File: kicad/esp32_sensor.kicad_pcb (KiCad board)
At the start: 4 copper layers, 66 x 58.4 mm, 51 parts

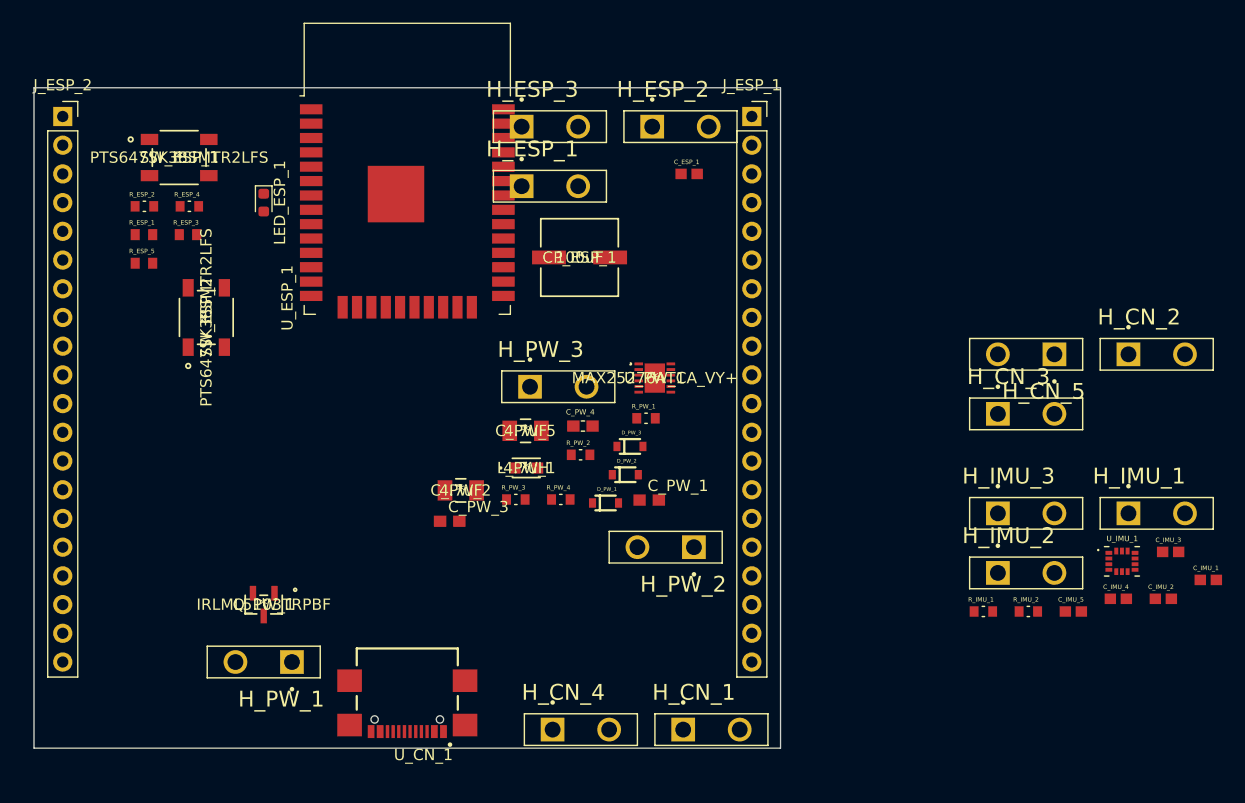
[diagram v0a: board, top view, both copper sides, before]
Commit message: Created PCB design for ESP32 sensor for v0.0.1. Exported PDFs and gerber files
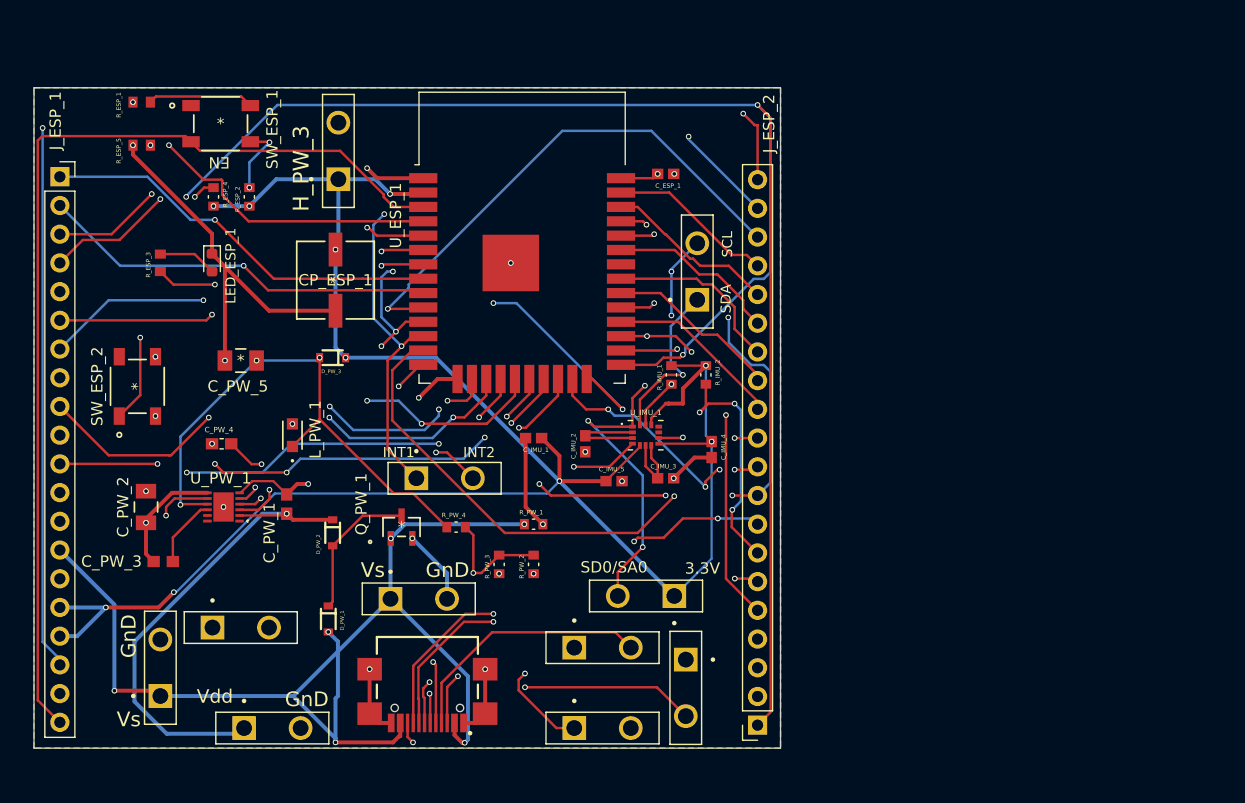
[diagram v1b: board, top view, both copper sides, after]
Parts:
- removed H_ESP_1, H_ESP_2, H_ESP_3: 1546931-2, footprints:1546931-2
- moved J_ESP_2 81.7 mm to (142.7, 125.0), turned to 180 degrees
- moved H_CN_3 79.8 mm to (89.9, 119.9), turned to 90 degrees
- moved H_CN_5 73.6 mm to (97.0, 116.3), turned to 0 degrees
- moved J_ESP_1 61.4 mm to (81.0, 76.5)
- moved C_IMU_1 61.0 mm to (122.9, 99.6), turned to 180 degrees
- moved C_IMU_2 52.9 mm to (127.5, 100.1), turned to 90 degrees
- moved H_IMU_2 52.1 mm to (115.1, 103.1)
- moved H_CN_2 51.1 mm to (136.4, 121.7), turned to 270 degrees
- moved H_IMU_1 45.9 mm to (137.4, 84.8), turned to 90 degrees
- moved C_IMU_3 45.1 mm to (134.6, 103.1)
- moved U_IMU_1 43.6 mm to (132.8, 99.3)
- moved C_IMU_5 42.2 mm to (130.0, 103.4)
- moved U_PW_1 39.8 mm to (95.5, 105.7), turned to 180 degrees
- moved C_IMU_4 38.3 mm to (138.7, 100.6), turned to 270 degrees
- moved H_PW_2 38.3 mm to (99.8, 125.2), turned to 0 degrees
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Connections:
- J_ESP_1 pad 17: Net-(J_ESP_1-Pad17) -> +3V3
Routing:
- net GND: track 0.00 -> 277.9 mm, vias 0 -> 15
- net +3V3: track 0.00 -> 179.0 mm, vias 0 -> 10
- net Net-(J_ESP_2-Pad1): track 0.00 -> 157.2 mm, vias 0 -> 4
- net Net-(C_ESP_1-Pad2): track 0.00 -> 127.5 mm, vias 0 -> 4
- net VS: track 0.00 -> 101.5 mm, vias 0 -> 6
- net /ESP32 Chip/IMU_SCL: track 0.00 -> 93.3 mm, vias 0 -> 6
- net /ESP32 Chip/IMU_INT2: track 0.00 -> 92.4 mm, vias 0 -> 8
- net /ESP32 Chip/IMU_INT1: track 0.00 -> 91.3 mm, vias 0 -> 4
- net Net-(J_ESP_1-Pad20): track 0.00 -> 89.3 mm
- net Net-(J_ESP_1-Pad19): track 0.00 -> 88.4 mm, vias 0 -> 1
- net Net-(J_ESP_1-Pad18): track 0.00 -> 88.3 mm, vias 0 -> 2
- net Net-(J_ESP_2-Pad3): track 0.00 -> 78.0 mm, vias 0 -> 3
- net /ESP32 Chip/IMU_SDA: track 0.00 -> 72.6 mm, vias 0 -> 5
- net Net-(J_ESP_2-Pad2): track 0.00 -> 55.5 mm, vias 0 -> 1
- net Net-(J_ESP_1-Pad7): track 0.00 -> 52.5 mm, vias 0 -> 2
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- added copper zone on B.Cu, net GND
- added copper zone on F.Cu, net GND
- added copper zone on In1.Cu, net GND
- added copper zone on In2.Cu, net GND
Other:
- net class Default: trace_width 0.25 -> 0.22; via_dia 0.8 -> 0.5; via_drill 0.4 -> 0.32
- net class Power added: clearance 0.2, trace_width 0.35, via_dia 0.5, via_drill 0.32
- rule via_min_size: 0.4 -> 0.5
- board text added: "3.3V"
- board text added: "Choong Jin Ng | jin8383@gmail.com"
- board text added: "EN"
- board text added: "ESP32 Sensor Module v0.0.1"
- board text added: "GnD"
- board text added: "INT1"
- board text added: "INT2"
- board text added: "Published on 23 November 2020"
- board text added: "SCL"
- board text added: "SD0/SA0"
- board text added: "SDA"
- board text added: "Vdd"
- board text added: "Vs"

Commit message: Updated schematic and PCB design to v0.0.2 for 2-layer pcb. Added more silkscreen text
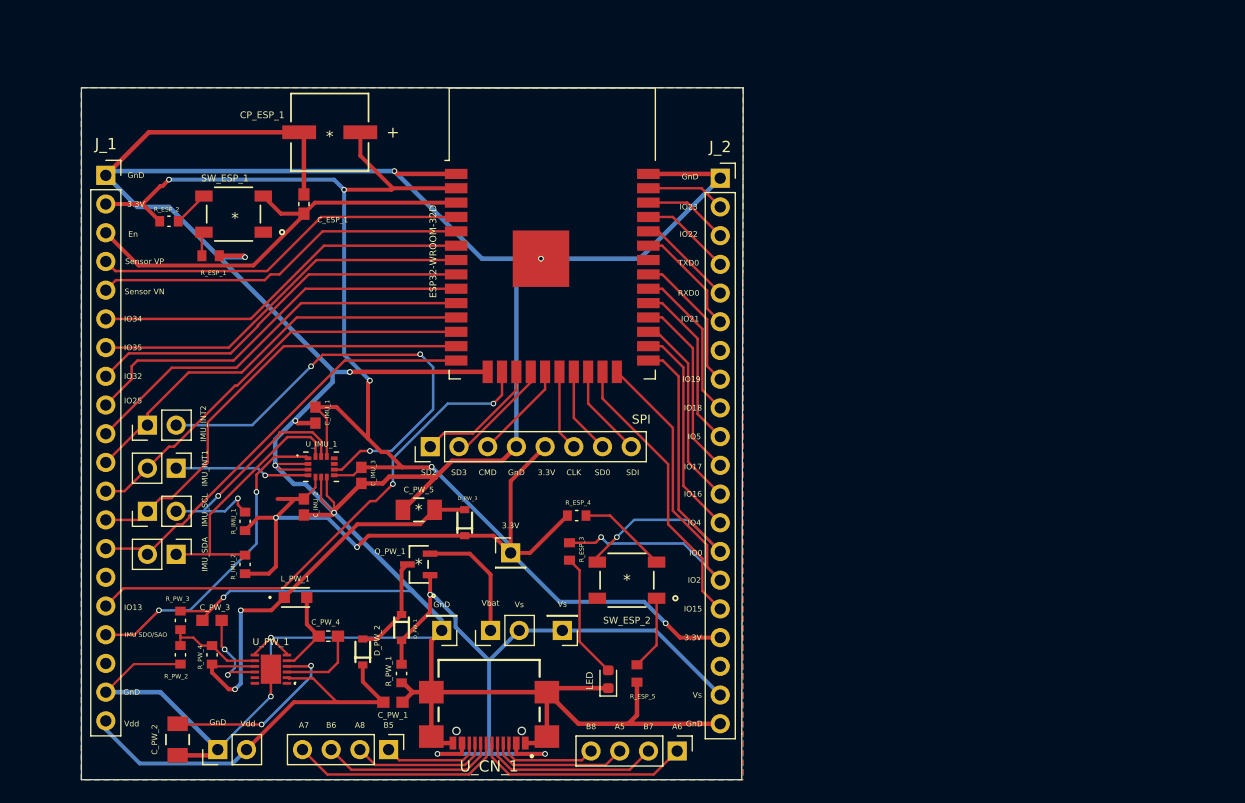
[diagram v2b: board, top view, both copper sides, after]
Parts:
- removed the C_IMU_2 at (127.5, 100.1)
- removed the C_IMU_3 at (134.6, 103.1)
- removed H_CN_1, H_CN_2, H_CN_3, H_CN_4, H_CN_5, H_IMU_1, H_IMU_2, H_IMU_3, H_PW_1, H_PW_2, H_PW_3: 1546931-2, footprints:1546931-2
- removed J_ESP_1, J_ESP_2: 4157, Connector_PinSocket_2.54mm:PinSocket_1x20_P2.54mm_Vertical
- added J_1: 4157, Connector_PinSocket_2.54mm:PinSocket_1x20_P2.54mm_Vertical, F.Cu at (85.1, 76.3)
- added J_2: 4157, Connector_PinSocket_2.54mm:PinSocket_1x20_P2.54mm_Vertical, F.Cu at (139.4, 76.6)
- added J_3: SPI, Connector_PinHeader_2.54mm:PinHeader_1x08_P2.54mm_Vertical, F.Cu at (113.8, 100.3)
- added J_4: IMU_INT2, Connector_PinHeader_2.54mm:PinHeader_1x02_P2.54mm_Vertical, F.Cu at (88.8, 98.4)
- added J_5: IMU_INT1, Connector_PinHeader_2.54mm:PinHeader_1x02_P2.54mm_Vertical, F.Cu at (91.3, 102.2)
- added J_6: IMU_SCL, Connector_PinHeader_2.54mm:PinHeader_1x02_P2.54mm_Vertical, F.Cu at (88.8, 106.0)
- added J_7: IMU_SDA, Connector_PinHeader_2.54mm:PinHeader_1x02_P2.54mm_Vertical, F.Cu at (91.3, 109.9)
- added J_CN_1: Header_Pin_4, Connector_PinHeader_2.54mm:PinHeader_1x04_P2.54mm_Vertical, F.Cu at (110.1, 127.1)
- added J_CN_2: Header_Pin_4, Connector_PinHeader_2.54mm:PinHeader_1x04_P2.54mm_Vertical, F.Cu at (135.6, 127.3)
- added J_CN_3: Vs, Connector_PinHeader_2.54mm:PinHeader_1x01_P2.54mm_Vertical, F.Cu at (125.5, 116.6)
- added J_CN_4: GnD, Connector_PinHeader_2.54mm:PinHeader_1x01_P2.54mm_Vertical, F.Cu at (114.8, 116.6)
- added J_PW_1: Header_Pin_2, Connector_PinHeader_2.54mm:PinHeader_1x02_P2.54mm_Vertical, F.Cu at (119.1, 116.6)
- added J_PW_2: Header_Pin_2, Connector_PinHeader_2.54mm:PinHeader_1x02_P2.54mm_Vertical, F.Cu at (95.0, 127.1)
- added J_PW_3: Header_Pin_1, Connector_PinHeader_2.54mm:PinHeader_1x01_P2.54mm_Vertical, F.Cu at (120.9, 109.7)
- C_ESP_1: value 100nF -> 0.1uF; footprint footprints:CAPC1608X90N -> footprints:CAPC1608X90
- moved R_ESP_5 64.1 mm to (132.1, 120.4), turned to 270 degrees
- moved LED_ESP_1 50.9 mm to (129.5, 120.9), turned to 90 degrees
- moved SW_ESP_2 46.6 mm to (131.2, 112.1), turned to 180 degrees
- moved R_ESP_3 44.3 mm to (126.1, 109.6), turned to 270 degrees
- moved R_IMU_2 44.1 mm to (97.4, 110.7), turned to 90 degrees
- moved R_ESP_4 42.7 mm to (126.7, 106.4), turned to 180 degrees
- moved R_IMU_1 39.9 mm to (97.4, 106.9), turned to 270 degrees
- moved C_IMU_2 36.4 mm to (102.6, 105.7)
- moved R_PW_2 32.3 mm to (91.7, 118.7)
- moved C_ESP_1 32.1 mm to (102.6, 78.9), turned to 90 degrees
- moved U_IMU_1 28.8 mm to (104.1, 102.1)
- moved R_PW_3 28.6 mm to (91.7, 115.7), turned to 270 degrees
- moved R_PW_4 24.4 mm to (94.5, 118.7), turned to 90 degrees
- moved C_IMU_3 22.4 mm to (107.7, 102.9), turned to 270 degrees
- moved C_PW_2 20.8 mm to (91.4, 126.2)
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- renumbered C_IMU_4 to C_IMU_2, C_IMU_5 to C_IMU_3
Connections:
- net Net-(J_ESP_2-Pad1) renamed /ESP32 Chip/ESP32_Pin25
- net Net-(J_ESP_2-Pad3) renamed /ESP32 Chip/ESP32_Pin24
- C_ESP_1 pad 1: GND -> /ESP32 Chip/ESP32_EN
- C_ESP_1 pad 2: Net-(C_ESP_1-Pad2) -> GND
- R_IMU_1 pad 1: /ESP32 Chip/IMU_SCL -> /IMU/IMU_SCL
- R_IMU_2 pad 2: /ESP32 Chip/IMU_SDA -> /IMU/IMU_SDA
- SW_ESP_1 pad 3: Net-(J_ESP_1-Pad20) -> /ESP32 Chip/ESP32_EN
- U_ESP_1 pad 1: Net-(C_ESP_1-Pad2) -> GND
- U_ESP_1 pad 10: Net-(J_ESP_2-Pad18) -> /ESP32 Chip/ESP32_Pin10
- U_ESP_1 pad 11: /ESP32 Chip/IMU_INT2 -> /ESP32 Chip/ESP32_Pin11
- U_ESP_1 pad 12: /ESP32 Chip/IMU_INT1 -> /ESP32 Chip/ESP32_Pin12
- U_ESP_1 pad 13: /ESP32 Chip/IMU_SCL -> /ESP32 Chip/ESP32_Pin13
- U_ESP_1 pad 14: /ESP32 Chip/IMU_SDA -> /ESP32 Chip/ESP32_Pin14
- U_ESP_1 pad 15: Net-(C_ESP_1-Pad2) -> GND
- U_ESP_1 pad 16: Net-(J_ESP_2-Pad8) -> /ESP32 Chip/ESP32_Pin16
- U_ESP_1 pad 17: Net-(J_ESP_1-Pad9) -> /ESP32 Chip/ESP32_Pin17
- U_ESP_1 pad 18: Net-(J_ESP_1-Pad8) -> /ESP32 Chip/ESP32_Pin18
- U_ESP_1 pad 19: Net-(J_ESP_1-Pad6) -> /ESP32 Chip/ESP32_Pin19
- U_ESP_1 pad 20: Net-(J_ESP_1-Pad7) -> /ESP32 Chip/ESP32_Pin20
- U_ESP_1 pad 21: Net-(J_ESP_1-Pad11) -> /ESP32 Chip/ESP32_Pin21
- U_ESP_1 pad 22: Net-(J_ESP_1-Pad10) -> /ESP32 Chip/ESP32_Pin22
- U_ESP_1 pad 23: Net-(J_ESP_2-Pad10) -> /ESP32 Chip/ESP32_Pin23
- U_ESP_1 pad 26: Net-(J_ESP_2-Pad5) -> /ESP32 Chip/ESP32_Pin26
- U_ESP_1 pad 27: /ESP32 Chip/IMU_SDO_SAO -> /ESP32 Chip/ESP32_Pin27
- U_ESP_1 pad 28: Net-(J_ESP_2-Pad12) -> /ESP32 Chip/ESP32_Pin28
- U_ESP_1 pad 29: Net-(J_ESP_2-Pad6) -> /ESP32 Chip/ESP32_Pin29
- U_ESP_1 pad 3: Net-(J_ESP_1-Pad20) -> /ESP32 Chip/ESP32_EN
- U_ESP_1 pad 30: Net-(J_ESP_2-Pad13) -> /ESP32 Chip/ESP32_Pin30
- U_ESP_1 pad 31: Net-(J_ESP_2-Pad14) -> /ESP32 Chip/ESP32_Pin31
- U_ESP_1 pad 33: Net-(J_ESP_2-Pad15) -> /ESP32 Chip/ESP32_Pin33
- U_ESP_1 pad 34: Net-(J_ESP_2-Pad4) -> /ESP32 Chip/ESP32_RX0
- U_ESP_1 pad 35: Net-(J_ESP_2-Pad2) -> /ESP32 Chip/ESP32_TX0
- U_ESP_1 pad 36: Net-(J_ESP_2-Pad16) -> /ESP32 Chip/ESP32_Pin36
- U_ESP_1 pad 37: Net-(J_ESP_2-Pad17) -> /ESP32 Chip/ESP32_Pin37
- U_ESP_1 pad 38: Net-(C_ESP_1-Pad2) -> GND
- U_ESP_1 pad 39: Net-(C_ESP_1-Pad2) -> GND
- U_ESP_1 pad 4: Net-(J_ESP_1-Pad19) -> /ESP32 Chip/ESP32_Pin4
- U_ESP_1 pad 5: Net-(J_ESP_1-Pad18) -> /ESP32 Chip/ESP32_Pin5
- U_ESP_1 pad 6: Net-(J_ESP_1-Pad3) -> /ESP32 Chip/ESP32_Pin6
- U_ESP_1 pad 7: Net-(J_ESP_1-Pad4) -> /ESP32 Chip/ESP32_Pin7
- U_ESP_1 pad 8: Net-(J_ESP_1-Pad1) -> /ESP32 Chip/ESP32_Pin8
- U_ESP_1 pad 9: Net-(J_ESP_1-Pad2) -> /ESP32 Chip/ESP32_Pin9
- U_IMU_1 pad 1: /ESP32 Chip/IMU_SDO_SAO -> /IMU/IMU_SDO_SAO
- U_IMU_1 pad 13: /ESP32 Chip/IMU_SCL -> /IMU/IMU_SCL
- U_IMU_1 pad 14: /ESP32 Chip/IMU_SDA -> /IMU/IMU_SDA
- U_IMU_1 pad 2: Net-(C_IMU_2-Pad2) -> GND
- U_IMU_1 pad 3: Net-(C_IMU_2-Pad2) -> GND
- U_IMU_1 pad 4: /ESP32 Chip/IMU_INT1 -> /IMU/IMU_INT1
- U_IMU_1 pad 6: Net-(C_IMU_3-Pad1) -> GND
- U_IMU_1 pad 7: Net-(C_IMU_3-Pad1) -> GND
- U_IMU_1 pad 9: /ESP32 Chip/IMU_INT2 -> /IMU/IMU_INT2
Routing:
- net Net-(C_ESP_1-Pad2): track 127.5 -> 0.00 mm, vias 4 -> 0
- net /ESP32 Chip/ESP32_Pin25: track 157.2 -> 34.1 mm, vias 4 -> 1
- net GND: track 277.9 -> 372.7 mm, vias 15 -> 10
- net /ESP32 Chip/IMU_SCL: track 93.3 -> 0.00 mm, vias 6 -> 0
- net /ESP32 Chip/IMU_INT2: track 92.4 -> 0.00 mm, vias 8 -> 0
- net /ESP32 Chip/IMU_INT1: track 91.3 -> 0.00 mm, vias 4 -> 0
- net Net-(J_ESP_1-Pad20): track 89.3 -> 0.00 mm
- net Net-(J_ESP_1-Pad19): track 88.4 -> 0.00 mm, vias 1 -> 0
- net Net-(J_ESP_1-Pad18): track 88.3 -> 0.00 mm, vias 2 -> 0
- net /ESP32 Chip/IMU_SDA: track 72.6 -> 0.00 mm, vias 5 -> 0
- net Net-(J_ESP_2-Pad2): track 55.5 -> 0.00 mm, vias 1 -> 0
- net Net-(J_ESP_1-Pad7): track 52.5 -> 0.00 mm, vias 2 -> 0
- net Net-(J_ESP_1-Pad10): track 49.7 -> 0.00 mm, vias 3 -> 0
- net /ESP32 Chip/IMU_SDO_SAO: track 49.1 -> 0.00 mm, vias 6 -> 0
- net Net-(J_ESP_1-Pad6): track 47.2 -> 0.00 mm, vias 3 -> 0
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- removed copper zone on In1.Cu, net GND
- removed copper zone on In2.Cu, net GND
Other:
- board size 66 x 58.4 mm -> 58.5 x 61.2 mm
- copper layers 4 -> 2
- net class GnD added: clearance 0.2, trace_width 0.4, via_dia 0.5, via_drill 0.32
- board text added: "ESP32 Sensor Module v0.0.2"
- board text added: "Published on 24 November 2020"
- board text removed: "3.3V"
- board text removed: "EN"
- board text removed: "ESP32 Sensor Module v0.0.1"
- board text removed: "GnD"
- board text removed: "INT1"
- board text removed: "INT2"
- board text removed: "Published on 23 November 2020"
- board text removed: "SCL"
- board text removed: "SD0/SA0"
- board text removed: "SDA"
- board text removed: "Vdd"
- board text removed: "Vs"

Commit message: Updated sensor module and PCB design to v0.0.3. Fixed design issues with USB. Updated via size to 0.6mm. Moved polarised capacitor towards inside the board
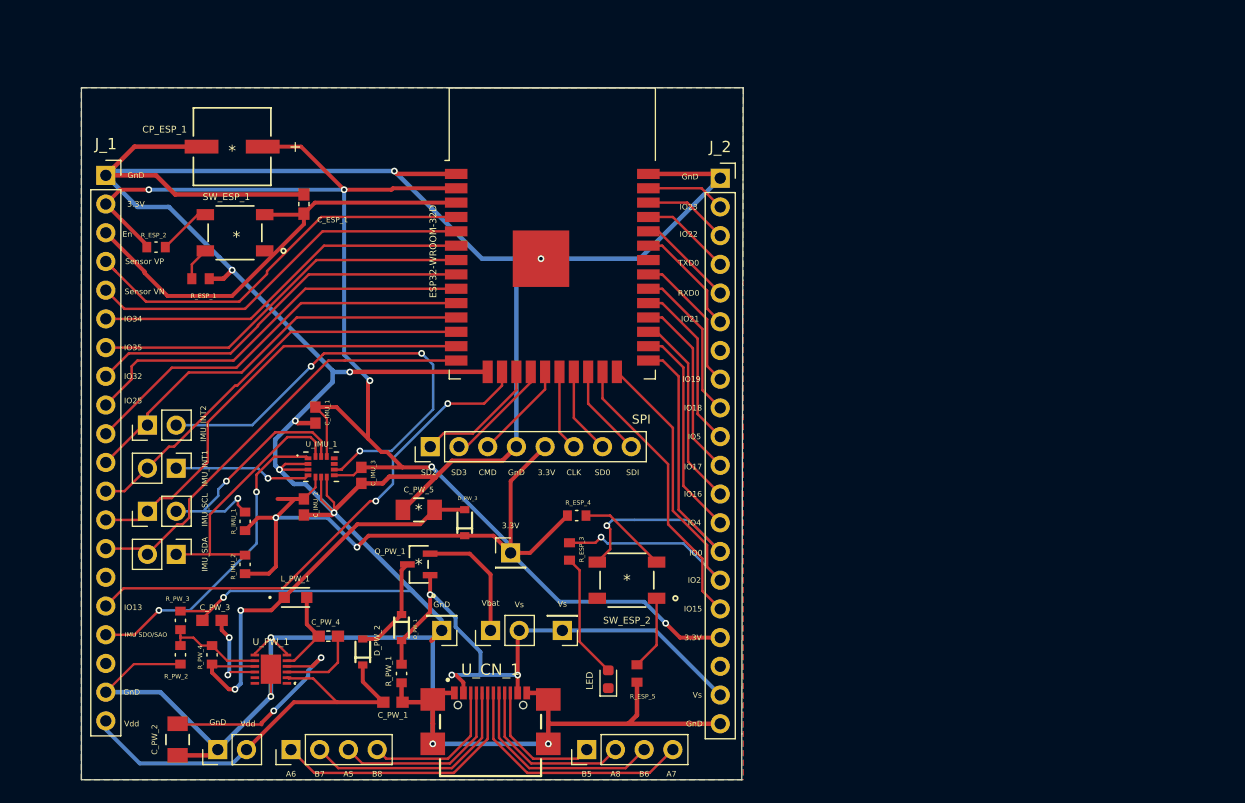
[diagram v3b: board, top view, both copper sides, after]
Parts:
- moved J_CN_2 34.2 mm to (101.5, 127.1), turned to 90 degrees
- moved J_CN_1 17.5 mm to (127.6, 127.1), turned to 90 degrees
- moved CP_ESP_1 8.73 mm to (96.3, 73.8)
- moved R_ESP_2 2.56 mm to (89.5, 82.7)
- moved U_CN_1 2.29 mm to (119.1, 123.2), turned to 0 degrees
- moved R_ESP_1 2.22 mm to (93.5, 85.5)
- moved SW_ESP_1 1.66 mm to (96.5, 81.4)
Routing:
- net VS: track 65.4 -> 51.8 mm
- net +3V3: track 178.3 -> 183.3 mm
- net Net-(J_CN_2-Pad2): track 15.7 -> 20.1 mm
- net Net-(J_CN_2-Pad4): track 8.80 -> 13.2 mm
- net Net-(J_CN_2-Pad3): track 12.2 -> 16.7 mm
- net Net-(J_CN_2-Pad1): track 19.1 -> 23.6 mm
- net /ESP32 Chip/ESP32_Pin4: track 33.3 -> 36.9 mm
- net Net-(J_CN_1-Pad3): track 15.6 -> 18.6 mm
- net Net-(J_CN_1-Pad2): track 12.2 -> 15.2 mm
- net Net-(J_CN_1-Pad1): track 8.72 -> 11.7 mm
- net Net-(J_CN_1-Pad4): track 19.1 -> 22.1 mm
- net /ESP32 Chip/ESP32_EN: track 38.8 -> 41.0 mm
- net Net-(C_PW_2-Pad1): track 16.7 -> 18.7 mm
- net Net-(R_ESP_2-Pad2): track 3.20 -> 4.73 mm
- net /ESP32 Chip/ESP32_Pin5: track 33.2 -> 34.5 mm
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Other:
- net class Default: via_dia 0.5 -> 0.6
- net class GnD: via_dia 0.5 -> 0.6
- net class Power: via_dia 0.5 -> 0.6
- rule via_min_size: 0.5 -> 0.6
- board text added: "ESP32 Sensor Module v0.0.3"
- board text added: "Published on 25 November 2020"
- board text removed: "ESP32 Sensor Module v0.0.2"
- board text removed: "Published on 24 November 2020"

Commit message: Fixed silkscreen to display properly. Moved header pin silkscreen to bottom
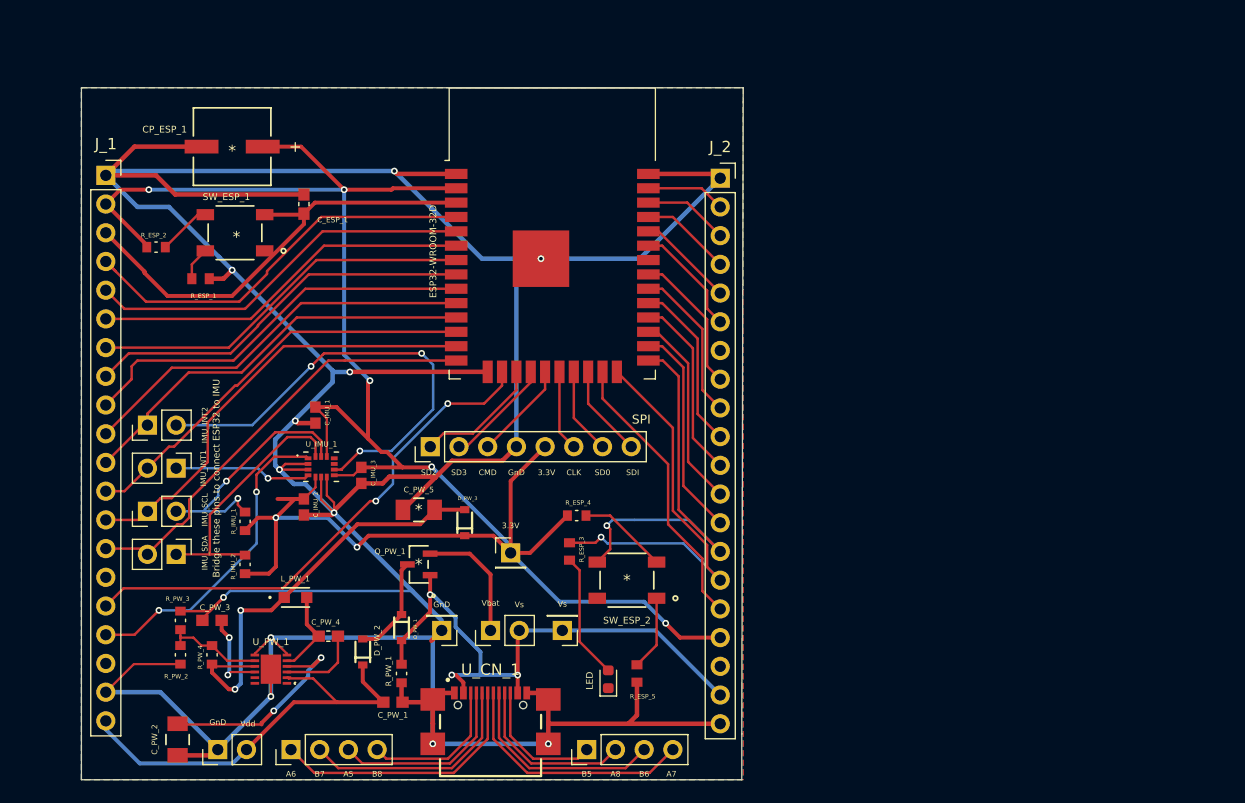
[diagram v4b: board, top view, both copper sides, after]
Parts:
- J_4: value IMU_INT2 -> Header_Pin_2
- J_5: value IMU_INT1 -> Header_Pin_2
- J_6: value IMU_SCL -> Header_Pin_2
- J_7: value IMU_SDA -> Header_Pin_2
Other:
- board text added: "Bridge these pins to connect ESP32 to IMU"
